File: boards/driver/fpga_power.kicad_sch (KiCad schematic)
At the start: 55 parts, among them J2 Barrel_Jack_Switch, J3 Conn_01x24, J4 Conn_01x24, Q87 IRF7413, U10 74LVC245, U11 74LVC245, U12 ADP151-3.3, U13 LTC4231-1, U14 74HC4514, U15 74LVC2G04, U16 74LVC2G04, U17 74LVC2G04, U18 74LVC2G04, U9 JTE0624D05

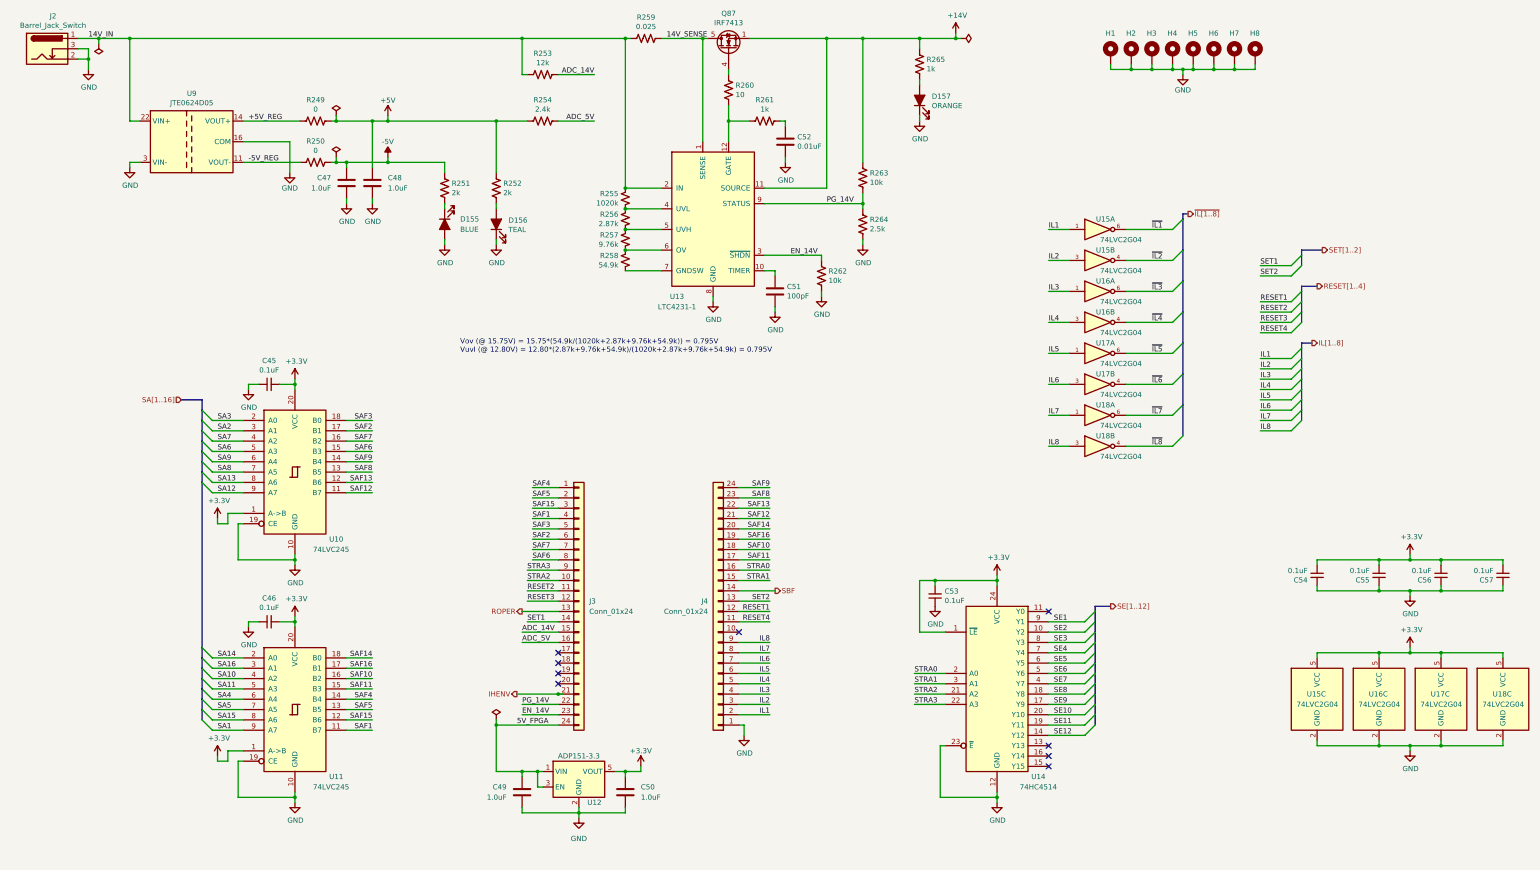
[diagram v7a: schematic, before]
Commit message: Driver: almost totally rearranged 3.3V logic section. The ratsnest is now significantly detangled, and the FPGA routing is almost done. 89 nets left.
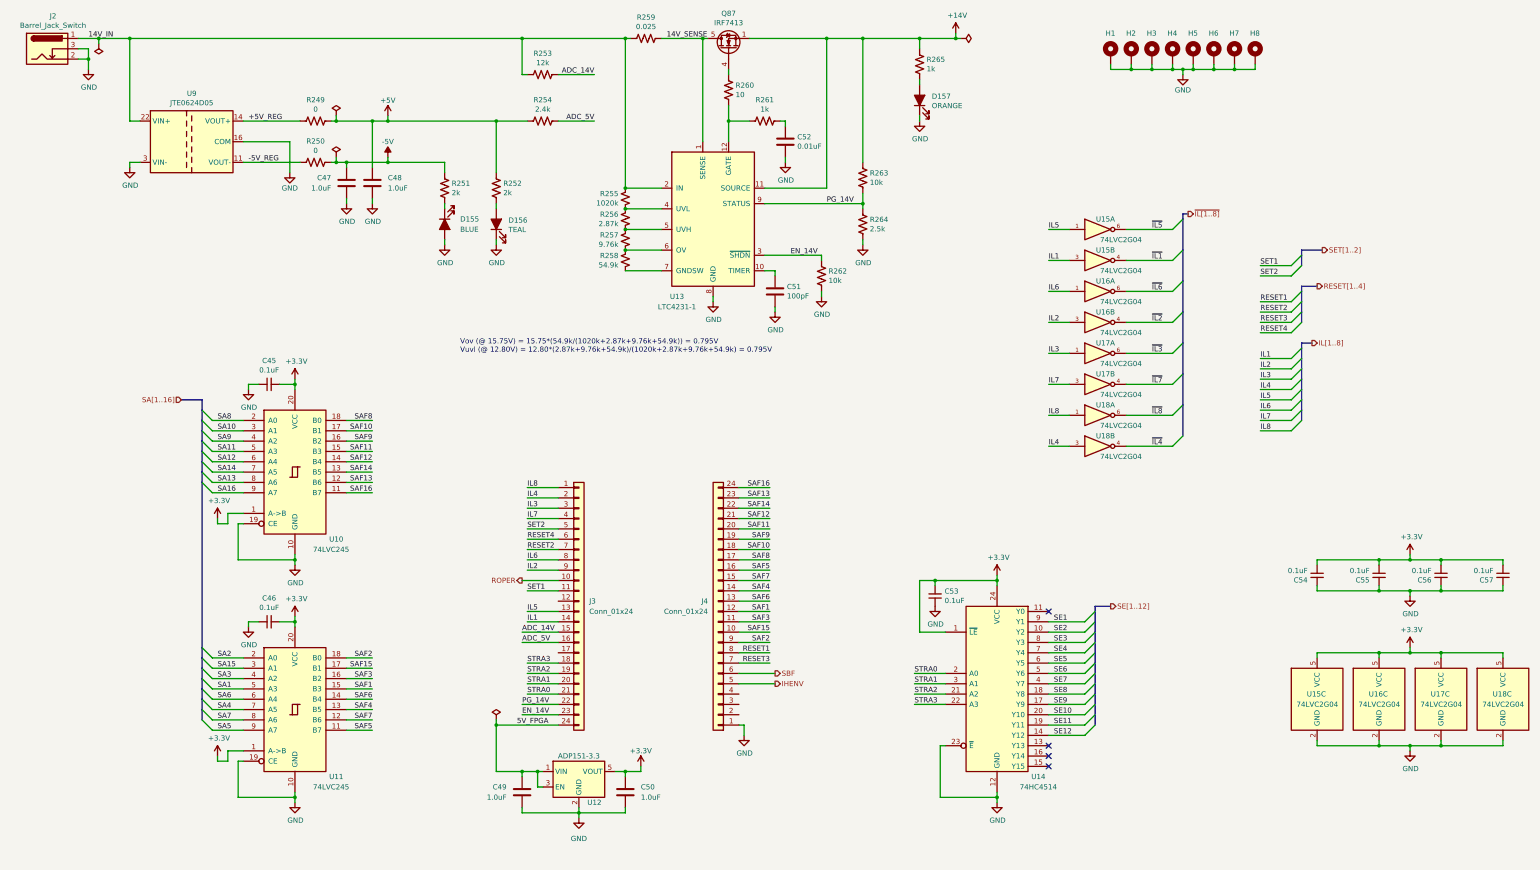
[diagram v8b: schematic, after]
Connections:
- net IHENV: now also J4.5 (Pin_5); no longer J3.21 (Pin_21)
- net IL1: now also J3.14 (Pin_14), U15.3; no longer J4.2 (Pin_2), U15.1
- net IL2: now also J3.9 (Pin_9), U16.3; no longer J4.3 (Pin_3), U15.3
- net IL3: now also J3.3 (Pin_3), U17.1; no longer J4.4 (Pin_4), U16.1
- net IL4: now also J3.2 (Pin_2), U18.3; no longer J4.5 (Pin_5), U16.3
- net IL5: now also J3.13 (Pin_13), U15.1; no longer J4.6 (Pin_6), U17.1
- net IL6: now also J3.8 (Pin_8), U16.1; no longer J4.7 (Pin_7), U17.3
- net IL7: now also J3.4 (Pin_4), U17.3; no longer J4.8 (Pin_8), U18.1
- net IL8: now also J3.1 (Pin_1), U18.1; no longer J4.9 (Pin_9), U18.3
- net RESET1: now also J4.8 (Pin_8); no longer J4.12 (Pin_12)
- net RESET2: now also J3.7 (Pin_7); no longer J3.11 (Pin_11)
- net RESET3: now also J4.7 (Pin_7); no longer J3.12 (Pin_12)
- net RESET4: now also J3.6 (Pin_6); no longer J4.11 (Pin_11)
- net ROPER: now also J3.10 (Pin_10); no longer J3.13 (Pin_13)
- net SA1: now also U11.5 (A3); no longer U11.9 (A7)
- net SA10: now also U10.3 (A1); no longer U11.4 (A2)
- net SA11: now also U10.5 (A3); no longer U11.5 (A3)
- net SA12: now also U10.6 (A4); no longer U10.9 (A7)
- net SA14: now also U10.7 (A5); no longer U11.2 (A0)
- net SA15: now also U11.3 (A1); no longer U11.8 (A6)
- net SA16: now also U10.9 (A7); no longer U11.3 (A1)
- net SA2: now also U11.2 (A0); no longer U10.3 (A1)
- net SA3: now also U11.4 (A2); no longer U10.2 (A0)
- net SA4: now also U11.7 (A5); no longer U11.6 (A4)
- net SA5: now also U11.9 (A7); no longer U11.7 (A5)
- net SA6: now also U11.6 (A4); no longer U10.5 (A3)
- net SA7: now also U11.8 (A6); no longer U10.4 (A2)
- net SA8: now also U10.2 (A0); no longer U10.7 (A5)
- net SA9: now also U10.4 (A2); no longer U10.6 (A4)
- net SAF1: now also J4.12 (Pin_12), U11.15 (B3); no longer J3.4 (Pin_4), U11.11 (B7)
- net SAF10: now also U10.17 (B1); no longer U11.16 (B2)
- net SAF11: now also J4.20 (Pin_20), U10.15 (B3); no longer J4.17 (Pin_17), U11.15 (B3)
- net SAF12: now also U10.14 (B4); no longer U10.11 (B7)
- net SAF13: now also J4.23 (Pin_23); no longer J4.22 (Pin_22)
- net SAF14: now also J4.22 (Pin_22), U10.13 (B5); no longer J4.20 (Pin_20), U11.18 (B0)
- net SAF15: now also J4.10 (Pin_10), U11.17 (B1); no longer J3.3 (Pin_3), U11.12 (B6)
- net SAF16: now also J4.24 (Pin_24), U10.11 (B7); no longer J4.19 (Pin_19), U11.17 (B1)
- net SAF2: now also J4.9 (Pin_9), U11.18 (B0); no longer J3.6 (Pin_6), U10.17 (B1)
- net SAF3: now also J4.11 (Pin_11), U11.16 (B2); no longer J3.5 (Pin_5), U10.18 (B0)
- net SAF4: now also J4.14 (Pin_14), U11.13 (B5); no longer J3.1 (Pin_1), U11.14 (B4)
- net SAF5: now also J4.16 (Pin_16), U11.11 (B7); no longer J3.2 (Pin_2), U11.13 (B5)
- net SAF6: now also J4.13 (Pin_13), U11.14 (B4); no longer J3.8 (Pin_8), U10.15 (B3)
- net SAF7: now also J4.15 (Pin_15), U11.12 (B6); no longer J3.7 (Pin_7), U10.16 (B2)
- net SAF8: now also J4.17 (Pin_17), U10.18 (B0); no longer J4.23 (Pin_23), U10.13 (B5)
- net SAF9: now also J4.19 (Pin_19), U10.16 (B2); no longer J4.24 (Pin_24), U10.14 (B4)
- net SBF: now also J4.6 (Pin_6); no longer J4.14 (Pin_14)
- net SET1: now also J3.11 (Pin_11); no longer J3.14 (Pin_14)
- net SET2: now also J3.5 (Pin_5); no longer J4.13 (Pin_13)
- net STRA0: now also J3.21 (Pin_21); no longer J4.16 (Pin_16)
- net STRA1: now also J3.20 (Pin_20); no longer J4.15 (Pin_15)
- net STRA2: now also J3.19 (Pin_19); no longer J3.10 (Pin_10)
- net STRA3: now also J3.18 (Pin_18); no longer J3.9 (Pin_9)
- net ~{IL1}: now also U15.4; no longer U15.6
- net ~{IL2}: now also U16.4; no longer U15.4
- net ~{IL3}: now also U17.6; no longer U16.6
- net ~{IL4}: now also U18.4; no longer U16.4
- net ~{IL5}: now also U15.6; no longer U17.6
- net ~{IL6}: now also U16.6; no longer U17.4
- net ~{IL7}: now also U17.4; no longer U18.6
- net ~{IL8}: now also U18.6; no longer U18.4
- no-connect marks 9 -> 4
